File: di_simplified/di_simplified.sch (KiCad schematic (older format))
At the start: 11 parts

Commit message: di simplified stuff
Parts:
- added R?: 10M, symbol R
- added U?: NE5532, symbol NE5532
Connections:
- wire segments 15 -> 24
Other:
- moved on the sheet: P?
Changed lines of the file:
@@
 L CONN_01X02 P?
 U 1 1 5744CF6D
-P 7000 3150
-F 0 "P?" H 6918 2868 50  0000 C CNN
-F 1 "CONN_01X02" H 6918 2960 50  0000 C CNN
-F 2 "" H 7000 3150 50  0000 C CNN
-F 3 "" H 7000 3150 50  0000 C CNN
-	1    7000 3150
+P 7150 3150
+F 0 "P?" H 7068 2868 50  0000 C CNN
+F 1 "CONN_01X02" H 7068 2960 50  0000 C CNN
+F 2 "" H 7150 3150 50  0000 C CNN
+F 3 "" H 7150 3150 50  0000 C CNN
+	1    7150 3150
 	1    0    0    1
 $EndComp
@@
 L GND #PWR?
 U 1 1 5744D515
-P 6800 3200
-F 0 "#PWR?" H 6800 2950 50  0001 C CNN
-F 1 "GND" H 6808 3026 50  0000 C CNN
-F 2 "" H 6800 3200 50  0000 C CNN
-F 3 "" H 6800 3200 50  0000 C CNN
-	1    6800 3200
+P 6950 3200
+F 0 "#PWR?" H 6950 2950 50  0001 C CNN
+F 1 "GND" H 6958 3026 50  0000 C CNN
+F 2 "" H 6950 3200 50  0000 C CNN
+F 3 "" H 6950 3200 50  0000 C CNN
+	1    6950 3200
 	1    0    0    -1
 $EndComp
@@
 Bias reference
 Wire Wire Line
-	3200 1900 3200 2000
-Wire Wire Line
-	3200 1950 4150 1950
+	3200 1900 3200 1950
+Wire Wire Line
+	3200 1950 3200 2000
+Wire Wire Line
+	3200 1950 3550 1950
+Wire Wire Line
+	3550 1950 4150 1950
 Connection ~ 3200 1950
 Wire Wire Line
-	4950 3200 5150 3200
+	4950 3200 5050 3200
+Wire Wire Line
+	5050 3200 5150 3200
 Wire Wire Line
 	5050 3200 5050 3650
@@
 	3600 3200 3700 3200
 Wire Wire Line
-	4000 3200 4650 3200
+	4000 3200 4150 3200
+Wire Wire Line
+	4150 3200 4650 3200
 Connection ~ 4150 3200
 Wire Wire Line
@@
 $EndComp
 Wire Wire Line
-	4150 1950 4150 2900
+	4150 1950 4150 2550
+Wire Wire Line
+	4150 2550 4150 2900
 Wire Wire Line
 	5150 3000 5000 3000
@@
 	5000 2550 4150 2550
 Connection ~ 4150 2550
+$Comp
+L NE5532 U?
+U 2 1 5746D07A
+P 6150 2000
+F 0 "U?" H 6491 2046 50  0000 L CNN
+F 1 "NE5532" H 6491 1954 50  0000 L CNN
+F 2 "" H 6150 2000 50  0000 C CNN
+F 3 "" H 6150 2000 50  0000 C CNN
+	2    6150 2000
+	1    0    0    -1
+$EndComp
+$Comp
+L +9V #PWR?
+U 1 1 5746D0C7
+P 6050 1700
+F 0 "#PWR?" H 6050 1550 50  0001 C CNN
+F 1 "+9V" H 6068 1874 50  0000 C CNN
+F 2 "" H 6050 1700 50  0000 C CNN
+F 3 "" H 6050 1700 50  0000 C CNN
+	1    6050 1700
+	1    0    0    -1
+$EndComp
+$Comp
+L GND #PWR?
+U 1 1 5746D0FF
+P 6050 2300
+F 0 "#PWR?" H 6050 2050 50  0001 C CNN
+F 1 "GND" H 6058 2126 50  0000 C CNN
+F 2 "" H 6050 2300 50  0000 C CNN
+F 3 "" H 6050 2300 50  0000 C CNN
+	1    6050 2300
+	1    0    0    -1
+$EndComp
+$Comp
+L GND #PWR?
+U 1 1 5746D137
+P 5750 2200
+F 0 "#PWR?" H 5750 1950 50  0001 C CNN
+F 1 "GND" H 5758 2026 50  0000 C CNN
+F 2 "" H 5750 2200 50  0000 C CNN
+F 3 "" H 5750 2200 50  0000 C CNN
+	1    5750 2200
+	1    0    0    -1
+$EndComp
+Wire Wire Line
+	5750 1900 5750 2100
+Wire Wire Line
+	5750 2100 5750 2200
+Wire Wire Line
+	5750 2100 5850 2100
+Wire Wire Line
+	5750 1900 5850 1900
+Connection ~ 5750 2100
+$Comp
+L R R?
+U 1 1 5746DC8A
+P 6600 3250
+F 0 "R?" H 6670 3296 50  0000 L CNN
+F 1 "10M" H 6670 3204 50  0000 L CNN
+F 2 "" V 6530 3250 50  0000 C CNN
+F 3 "" H 6600 3250 50  0000 C CNN
+	1    6600 3250
+	1    0    0    -1
+$EndComp
+Connection ~ 6600 3100
+$Comp
+L GND #PWR?
+U 1 1 5746DCDB
+P 6600 3400
+F 0 "#PWR?" H 6600 3150 50  0001 C CNN
+F 1 "GND" H 6608 3226 50  0000 C CNN
+F 2 "" H 6600 3400 50  0000 C CNN
+F 3 "" H 6600 3400 50  0000 C CNN
+	1    6600 3400
+	1    0    0    -1
+$EndComp
 $EndSCHEMATC

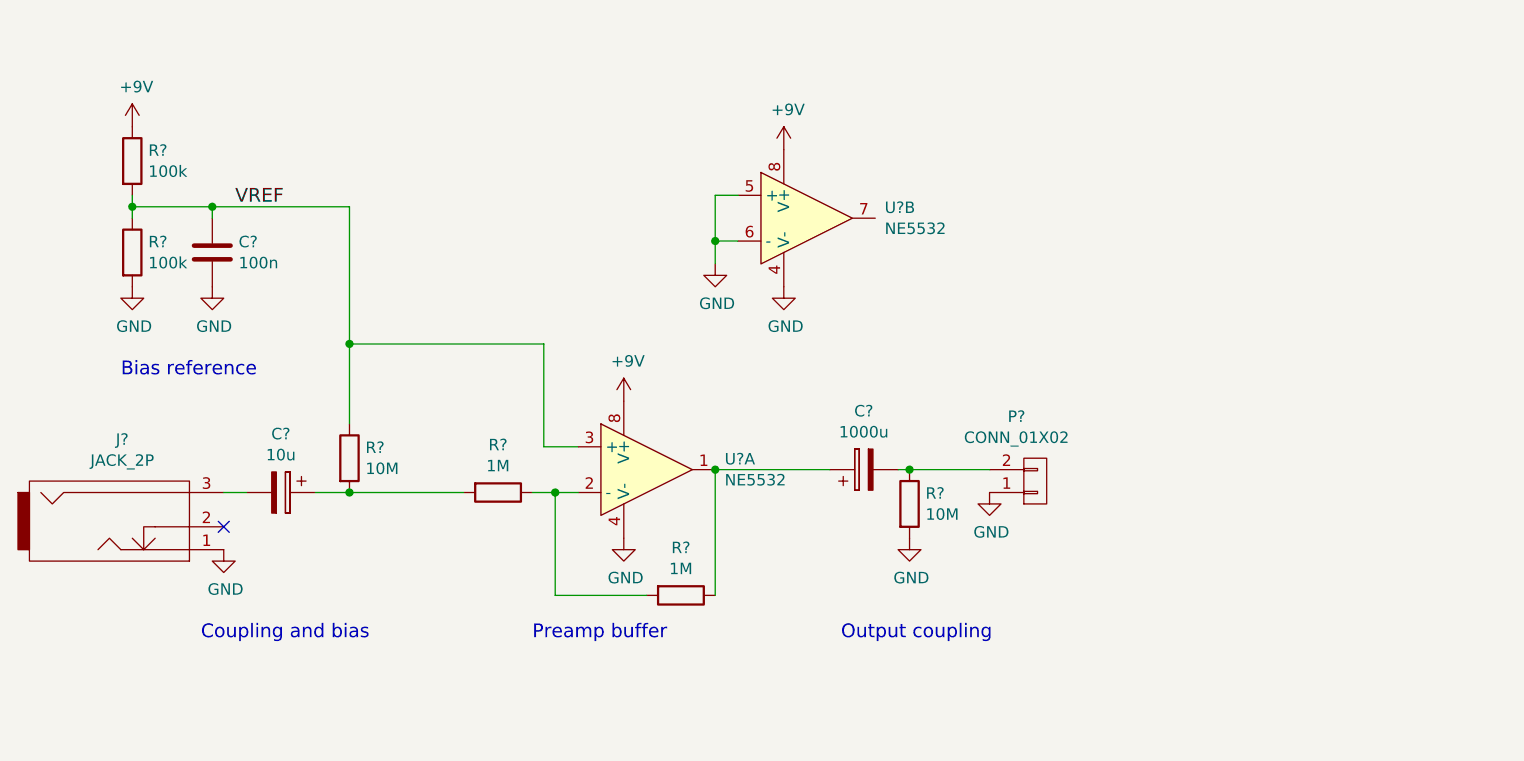
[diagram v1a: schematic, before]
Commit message: Split rails, direct coupled input/output
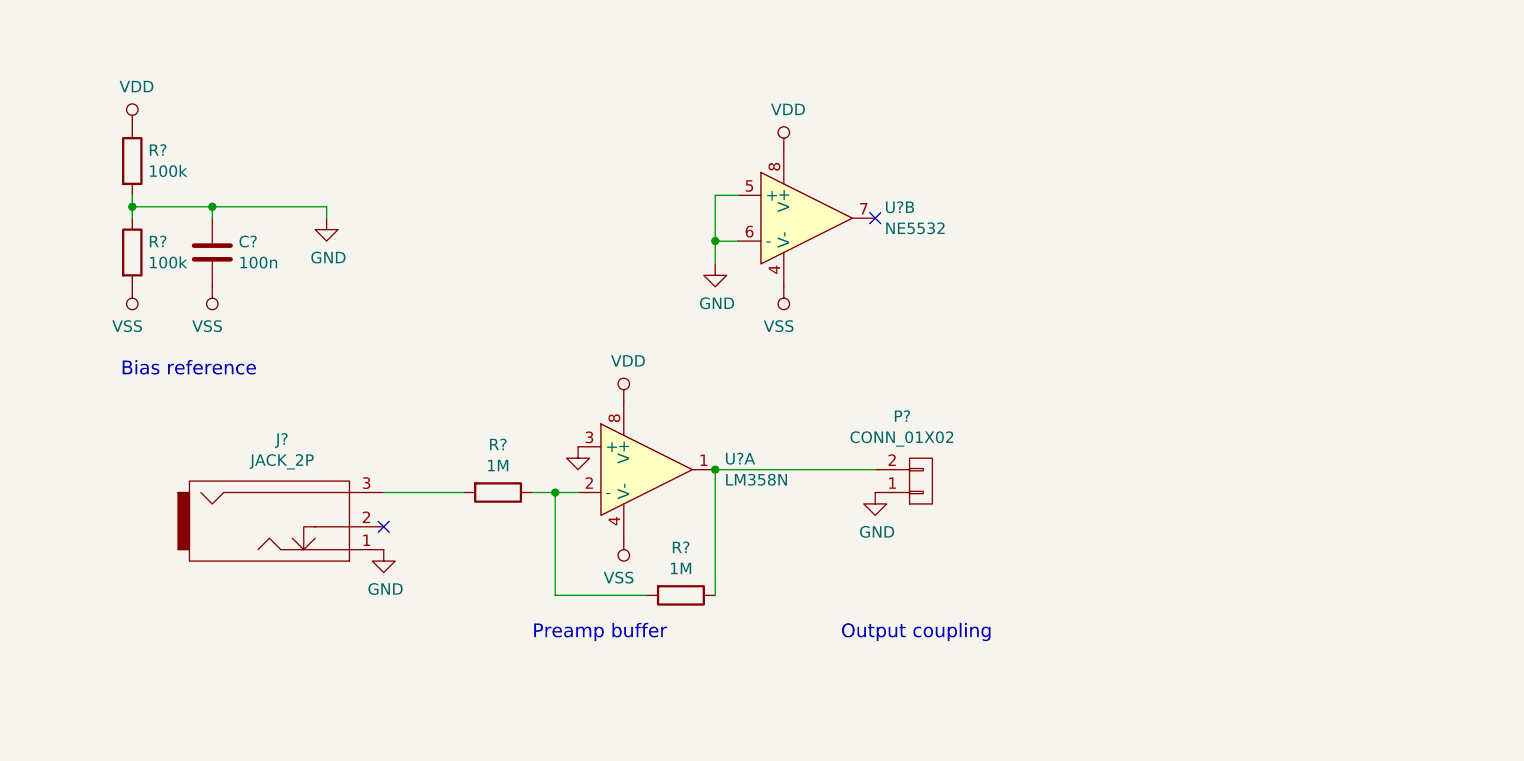
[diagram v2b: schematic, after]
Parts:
- removed C?: 10u, symbol CP
- removed C?: 1000u, symbol CP
- removed R? (x2): 10M, symbol R
- U?: value NE5532 -> LM358N
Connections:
- net VREF is gone; now on net GND: C?.1, R?.1, R?.2, U?.3 (+)
- net GND: no longer C?.2, R?.2, U?.4 (V-), U?.4 (V-)
- net at J?.3: now also R?.2
- net at P?.2 (P2): now also R?.1, U?.1
- net +9V renamed VDD
- new net VSS: C?.2, R?.2, U?.4 (V-), U?.4 (V-)
- no-connect marks 1 -> 2
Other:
- note removed: "Coupling and bias"
- moved on the sheet: J?, P?
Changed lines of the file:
@@
 L JACK_2P J?
 U 1 1 5744CF3C
-P 3150 3350
-F 0 "J?" H 3156 3732 50  0000 C CNN
-F 1 "JACK_2P" H 3156 3640 50  0000 C CNN
-F 2 "" H 3150 3350 50  0000 C CNN
-F 3 "" H 3150 3350 50  0000 C CNN
-	1    3150 3350
+P 3850 3350
+F 0 "J?" H 3856 3732 50  0000 C CNN
+F 1 "JACK_2P" H 3856 3640 50  0000 C CNN
+F 2 "" H 3850 3350 50  0000 C CNN
+F 3 "" H 3850 3350 50  0000 C CNN
+	1    3850 3350
 	1    0    0    -1
 $EndComp
@@
 L CONN_01X02 P?
 U 1 1 5744CF6D
-P 7150 3150
-F 0 "P?" H 7068 2868 50  0000 C CNN
-F 1 "CONN_01X02" H 7068 2960 50  0000 C CNN
-F 2 "" H 7150 3150 50  0000 C CNN
-F 3 "" H 7150 3150 50  0000 C CNN
-	1    7150 3150
+P 6650 3150
+F 0 "P?" H 6568 2868 50  0000 C CNN
+F 1 "CONN_01X02" H 6568 2960 50  0000 C CNN
+F 2 "" H 6650 3150 50  0000 C CNN
+F 3 "" H 6650 3150 50  0000 C CNN
+	1    6650 3150
 	1    0    0    1
-$EndComp
-$Comp
-L +9V #PWR?
-U 1 1 5744D12B
-P 3200 1600
-F 0 "#PWR?" H 3200 1450 50  0001 C CNN
-F 1 "+9V" H 3218 1774 50  0000 C CNN
-F 2 "" H 3200 1600 50  0000 C CNN
-F 3 "" H 3200 1600 50  0000 C CNN
-	1    3200 1600
-	1    0    0    -1
 $EndComp
 $Comp
@@
 $Comp
 L GND #PWR?
-U 1 1 5744D1E6
-P 3200 2300
-F 0 "#PWR?" H 3200 2050 50  0001 C CNN
-F 1 "GND" H 3208 2126 50  0000 C CNN
-F 2 "" H 3200 2300 50  0000 C CNN
-F 3 "" H 3200 2300 50  0000 C CNN
-	1    3200 2300
-	1    0    0    -1
-$EndComp
-Text Label 3650 1950 0    60   ~ 0
-VREF
-$Comp
-L GND #PWR?
-U 1 1 5744D4EF
-P 3600 3450
-F 0 "#PWR?" H 3600 3200 50  0001 C CNN
-F 1 "GND" H 3608 3276 50  0000 C CNN
-F 2 "" H 3600 3450 50  0000 C CNN
-F 3 "" H 3600 3450 50  0000 C CNN
-	1    3600 3450
-	1    0    0    -1
-$EndComp
-$Comp
-L GND #PWR?
 U 1 1 5744D515
-P 6950 3200
-F 0 "#PWR?" H 6950 2950 50  0001 C CNN
-F 1 "GND" H 6958 3026 50  0000 C CNN
-F 2 "" H 6950 3200 50  0000 C CNN
-F 3 "" H 6950 3200 50  0000 C CNN
-	1    6950 3200
-	1    0    0    -1
-$EndComp
-NoConn ~ 3600 3350
+P 6450 3200
+F 0 "#PWR?" H 6450 2950 50  0001 C CNN
+F 1 "GND" H 6458 3026 50  0000 C CNN
+F 2 "" H 6450 3200 50  0000 C CNN
+F 3 "" H 6450 3200 50  0000 C CNN
+	1    6450 3200
+	1    0    0    -1
+$EndComp
+NoConn ~ 4300 3350
 $Comp
 L R R?
@@
 $EndComp
 $Comp
-L GND #PWR?
-U 1 1 5744D7F7
-P 5350 3400
-F 0 "#PWR?" H 5350 3150 50  0001 C CNN
-F 1 "GND" H 5358 3226 50  0000 C CNN
-F 2 "" H 5350 3400 50  0000 C CNN
-F 3 "" H 5350 3400 50  0000 C CNN
-	1    5350 3400
-	1    0    0    -1
-$EndComp
-$Comp
-L +9V #PWR?
-U 1 1 5744D823
-P 5350 2800
-F 0 "#PWR?" H 5350 2650 50  0001 C CNN
-F 1 "+9V" H 5368 2974 50  0000 C CNN
-F 2 "" H 5350 2800 50  0000 C CNN
-F 3 "" H 5350 2800 50  0000 C CNN
-	1    5350 2800
-	1    0    0    -1
-$EndComp
-$Comp
 L R R?
 U 1 1 5744DCBA
@@
 	0    1    1    0
 $EndComp
-$Comp
-L CP C?
-U 1 1 5744E1F2
-P 3850 3200
-F 0 "C?" V 3594 3200 50  0000 C CNN
-F 1 "10u" V 3686 3200 50  0000 C CNN
-F 2 "" H 3888 3050 50  0000 C CNN
-F 3 "" H 3850 3200 50  0000 C CNN
-	1    3850 3200
-	0    1    1    0
-$EndComp
-$Comp
-L R R?
-U 1 1 5744E4D1
-P 4150 3050
-F 0 "R?" H 4220 3096 50  0000 L CNN
-F 1 "10M" H 4220 3004 50  0000 L CNN
-F 2 "" V 4080 3050 50  0000 C CNN
-F 3 "" H 4150 3050 50  0000 C CNN
-	1    4150 3050
-	1    0    0    -1
-$EndComp
-Text Notes 3500 3850 0    60   ~ 0
-Coupling and bias
 Text Notes 4950 3850 0    60   ~ 0
 Preamp buffer
-$Comp
-L CP C?
-U 1 1 5744EC93
-P 6400 3100
-F 0 "C?" V 6656 3100 50  0000 C CNN
-F 1 "1000u" V 6564 3100 50  0000 C CNN
-F 2 "" H 6438 2950 50  0000 C CNN
-F 3 "" H 6400 3100 50  0000 C CNN
-	1    6400 3100
-	0    -1   -1   0
-$EndComp
 Text Notes 6300 3850 0    60   ~ 0
 Output coupling
@@
 	3200 1950 3550 1950
 Wire Wire Line
-	3550 1950 4150 1950
+	3550 1950 4050 1950
 Connection ~ 3200 1950
 Wire Wire Line
@@
 	5050 3650 5450 3650
 Wire Wire Line
-	3600 3200 3700 3200
-Wire Wire Line
-	4000 3200 4150 3200
-Wire Wire Line
-	4150 3200 4650 3200
-Connection ~ 4150 3200
-Wire Wire Line
-	6550 3100 6950 3100
-Wire Wire Line
-	5750 3100 6250 3100
+	4300 3200 4650 3200
+Wire Wire Line
+	5750 3100 6450 3100
 $Comp
 L NE5532 U?
@@
 P 5450 3100
 F 0 "U?" H 5791 3146 50  0000 L CNN
-F 1 "NE5532" H 5791 3054 50  0000 L CNN
+F 1 "LM358N" H 5791 3054 50  0000 L CNN
 F 2 "" H 5450 3100 50  0000 C CNN
 F 3 "" H 5450 3100 50  0000 C CNN
@@
 Connection ~ 3550 1950
 $Comp
-L GND #PWR?
-U 1 1 57450604
-P 3550 2300
-F 0 "#PWR?" H 3550 2050 50  0001 C CNN
-F 1 "GND" H 3558 2126 50  0000 C CNN
-F 2 "" H 3550 2300 50  0000 C CNN
-F 3 "" H 3550 2300 50  0000 C CNN
-	1    3550 2300
-	1    0    0    -1
-$EndComp
-Wire Wire Line
-	4150 1950 4150 2550
-Wire Wire Line
-	4150 2550 4150 2900
-Wire Wire Line
-	5150 3000 5000 3000
-Wire Wire Line
-	5000 3000 5000 2550
-Wire Wire Line
-	5000 2550 4150 2550
-Connection ~ 4150 2550
-$Comp
 L NE5532 U?
 U 2 1 5746D07A
@@
 $EndComp
 $Comp
-L +9V #PWR?
-U 1 1 5746D0C7
-P 6050 1700
-F 0 "#PWR?" H 6050 1550 50  0001 C CNN
-F 1 "+9V" H 6068 1874 50  0000 C CNN
-F 2 "" H 6050 1700 50  0000 C CNN
-F 3 "" H 6050 1700 50  0000 C CNN
-	1    6050 1700
-	1    0    0    -1
-$EndComp
-$Comp
-L GND #PWR?
-U 1 1 5746D0FF
-P 6050 2300
-F 0 "#PWR?" H 6050 2050 50  0001 C CNN
-F 1 "GND" H 6058 2126 50  0000 C CNN
-F 2 "" H 6050 2300 50  0000 C CNN
-F 3 "" H 6050 2300 50  0000 C CNN
-	1    6050 2300
-	1    0    0    -1
-$EndComp
-$Comp
 L GND #PWR?
 U 1 1 5746D137
@@
 Connection ~ 5750 2100
 $Comp
-L R R?
-U 1 1 5746DC8A
-P 6600 3250
-F 0 "R?" H 6670 3296 50  0000 L CNN
-F 1 "10M" H 6670 3204 50  0000 L CNN
-F 2 "" V 6530 3250 50  0000 C CNN
-F 3 "" H 6600 3250 50  0000 C CNN
-	1    6600 3250
-	1    0    0    -1
-$EndComp
-Connection ~ 6600 3100
-$Comp
-L GND #PWR?
-U 1 1 5746DCDB
-P 6600 3400
-F 0 "#PWR?" H 6600 3150 50  0001 C CNN
-F 1 "GND" H 6608 3226 50  0000 C CNN
-F 2 "" H 6600 3400 50  0000 C CNN
-F 3 "" H 6600 3400 50  0000 C CNN
-	1    6600 3400
-	1    0    0    -1
-$EndComp
+L GND #PWR?
+U 1 1 5744D4EF
+P 4300 3450
+F 0 "#PWR?" H 4300 3200 50  0001 C CNN
+F 1 "GND" H 4308 3276 50  0000 C CNN
+F 2 "" H 4300 3450 50  0000 C CNN
+F 3 "" H 4300 3450 50  0000 C CNN
+	1    4300 3450
+	1    0    0    -1
+$EndComp
+$Comp
+L GND #PWR?
+U 1 1 5748440B
+P 4050 2000
+F 0 "#PWR?" H 4050 1750 50  0001 C CNN
+F 1 "GND" H 4058 1826 50  0000 C CNN
+F 2 "" H 4050 2000 50  0000 C CNN
+F 3 "" H 4050 2000 50  0000 C CNN
+	1    4050 2000
+	1    0    0    -1
+$EndComp
+Wire Wire Line
+	4050 1950 4050 2000
+$Comp
+L VSS #PWR?
+U 1 1 57484564
+P 3200 2300
+F 0 "#PWR?" H 3200 2150 50  0001 C CNN
+F 1 "VSS" H 3221 2474 50  0000 C CNN
+F 2 "" H 3200 2300 50  0000 C CNN
+F 3 "" H 3200 2300 50  0000 C CNN
+	1    3200 2300
+	-1   0    0    1
+$EndComp
+$Comp
+L VDD #PWR?
+U 1 1 57484615
+P 3200 1600
+F 0 "#PWR?" H 3200 1450 50  0001 C CNN
+F 1 "VDD" H 3220 1774 50  0000 C CNN
+F 2 "" H 3200 1600 50  0000 C CNN
+F 3 "" H 3200 1600 50  0000 C CNN
+	1    3200 1600
+	1    0    0    -1
+$EndComp
+$Comp
+L VSS #PWR?
+U 1 1 57484650
+P 3550 2300
+F 0 "#PWR?" H 3550 2150 50  0001 C CNN
+F 1 "VSS" H 3571 2474 50  0000 C CNN
+F 2 "" H 3550 2300 50  0000 C CNN
+F 3 "" H 3550 2300 50  0000 C CNN
+	1    3550 2300
+	-1   0    0    1
+$EndComp
+$Comp
+L GND #PWR?
+U 1 1 57484A9B
+P 5150 3000
+F 0 "#PWR?" H 5150 2750 50  0001 C CNN
+F 1 "GND" H 5158 2826 50  0001 C CNN
+F 2 "" H 5150 3000 50  0000 C CNN
+F 3 "" H 5150 3000 50  0000 C CNN
+	1    5150 3000
+	1    0    0    -1
+$EndComp
+$Comp
+L VSS #PWR?
+U 1 1 57484F59
+P 6050 2300
+F 0 "#PWR?" H 6050 2150 50  0001 C CNN
+F 1 "VSS" H 6071 2474 50  0000 C CNN
+F 2 "" H 6050 2300 50  0000 C CNN
+F 3 "" H 6050 2300 50  0000 C CNN
+	1    6050 2300
+	-1   0    0    1
+$EndComp
+$Comp
+L VDD #PWR?
+U 1 1 57484FC8
+P 6050 1700
+F 0 "#PWR?" H 6050 1550 50  0001 C CNN
+F 1 "VDD" H 6070 1874 50  0000 C CNN
+F 2 "" H 6050 1700 50  0000 C CNN
+F 3 "" H 6050 1700 50  0000 C CNN
+	1    6050 1700
+	1    0    0    -1
+$EndComp
+$Comp
+L VDD #PWR?
+U 1 1 57485001
+P 5350 2800
+F 0 "#PWR?" H 5350 2650 50  0001 C CNN
+F 1 "VDD" H 5370 2974 50  0000 C CNN
+F 2 "" H 5350 2800 50  0000 C CNN
+F 3 "" H 5350 2800 50  0000 C CNN
+	1    5350 2800
+	1    0    0    -1
+$EndComp
+$Comp
+L VSS #PWR?
+U 1 1 57485030
+P 5350 3400
+F 0 "#PWR?" H 5350 3250 50  0001 C CNN
+F 1 "VSS" H 5371 3574 50  0000 C CNN
+F 2 "" H 5350 3400 50  0000 C CNN
+F 3 "" H 5350 3400 50  0000 C CNN
+	1    5350 3400
+	-1   0    0    1
+$EndComp
+NoConn ~ 6450 2000
 $EndSCHEMATC

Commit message: schematic fiddling
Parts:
- added P?: LEFT, symbol CONN_01X02
- added R? (x2): 2k2, symbol R
- added R? (x2): 22k, symbol R
- added U? (x2): NE5532, symbol NE5532
- P?: value CONN_01X02 -> RIGHT
- U?: value NE5532 -> LM358N
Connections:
- net GND: now also P?.1 (P1), U?.3 (+), U?.5 (+)
- net VDD: now also U?.8 (V+), U?.8 (V+)
- net VSS: now also U?.4 (V-), U?.4 (V-)
- net at R?.1, U?.1: now also R?.2, R?.2; no longer P?.2 (P2)
- new net: P?.2 (P2), R?.1, U?.7
- new net: P?.2 (P2), R?.1, U?.1
- new net: R?.1, R?.2, U?.2 (-)
- new net: R?.1, R?.2, U?.6 (-)
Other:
- note removed: "Output coupling"
- moved on the sheet: P?, U?B
